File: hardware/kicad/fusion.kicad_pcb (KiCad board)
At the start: 2 copper layers, 0 parts

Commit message: 0603 footprints and SP3T
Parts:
- added C1: 4.7uF, Capacitor_SMD:C_0603_1608Metric_Pad1.08x0.95mm_HandSolder, F.Cu at (206.2, 99.8)
- added C2: 4.7uF, Capacitor_SMD:C_0603_1608Metric_Pad1.08x0.95mm_HandSolder, F.Cu at (201.3, 102.8)
- added C3: 0.1uF, Capacitor_SMD:C_0603_1608Metric_Pad1.08x0.95mm_HandSolder, F.Cu at (206.1, 102.8)
- added C4: 0.1uF, Capacitor_SMD:C_0603_1608Metric_Pad1.08x0.95mm_HandSolder, F.Cu at (196.5, 102.6)
- added C5: 0.1uF, Capacitor_SMD:C_0603_1608Metric_Pad1.08x0.95mm_HandSolder, F.Cu at (201.3, 105.8)
- added C6: 0.1uF, Capacitor_SMD:C_0603_1608Metric_Pad1.08x0.95mm_HandSolder, F.Cu at (196.5, 105.6)
- added C7: 0.1uF, Capacitor_SMD:C_0603_1608Metric_Pad1.08x0.95mm_HandSolder, F.Cu at (201.4, 99.8)
- added C8: 0.1uF, Capacitor_SMD:C_0603_1608Metric_Pad1.08x0.95mm_HandSolder, F.Cu at (196.5, 108.6)
- added D1: LED, LED_SMD:LED_0603_1608Metric_Pad1.05x0.95mm_HandSolder, F.Cu at (211.1, 99.8)
- added D2: LED, LED_SMD:LED_0603_1608Metric_Pad1.05x0.95mm_HandSolder, F.Cu at (201.4, 108.9)
- added J1: BATTERY, Fusion:JST, F.Cu at (187.5, 108.0)
- added J2: LSM6DSOX, Connector_PinHeader_2.54mm:PinHeader_1x06_P2.54mm_Horizontal, F.Cu at (173.7, 73.4)
- added J3: PICKIT, Connector_PinSocket_2.54mm:PinSocket_1x05_P2.54mm_Vertical, F.Cu at (189.7, 90.8)
- added J4: HC-05, Connector_PinHeader_2.54mm:PinHeader_1x05_P2.54mm_Horizontal, F.Cu at (192.9, 73.2)
- added J5: FLEX, Connector_PinHeader_2.54mm:PinHeader_2x05_P2.54mm_Horizontal, F.Cu at (173.7, 90.8)
- added J7: FTDI, Connector_PinSocket_2.54mm:PinSocket_1x06_P2.54mm_Vertical, F.Cu at (187.1, 73.4)
- added L1: 4.7uH, Inductor_SMD:L_0603_1608Metric_Pad1.05x0.95mm_HandSolder, F.Cu at (196.6, 99.7)
- added R1: 270R, Resistor_SMD:R_0603_1608Metric_Pad0.98x0.95mm_HandSolder, F.Cu at (197.6, 91.9)
- added R10: 10K, Resistor_SMD:R_0603_1608Metric_Pad0.98x0.95mm_HandSolder, F.Cu at (210.9, 102.8)
- added R2: 20K, Resistor_SMD:R_0603_1608Metric_Pad0.98x0.95mm_HandSolder, F.Cu at (203.7, 94.7)
- added R3: 10K, Resistor_SMD:R_0603_1608Metric_Pad0.98x0.95mm_HandSolder, F.Cu at (204.5, 91.8)
- added R4: 270R, Resistor_SMD:R_0603_1608Metric_Pad0.98x0.95mm_HandSolder, F.Cu at (210.9, 108.8)
- added R5: 10K, Resistor_SMD:R_0603_1608Metric_Pad0.98x0.95mm_HandSolder, F.Cu at (215.8, 99.8)
- added R6: 10K, Resistor_SMD:R_0603_1608Metric_Pad0.98x0.95mm_HandSolder, F.Cu at (215.7, 102.8)
- added R7: 10K, Resistor_SMD:R_0603_1608Metric_Pad0.98x0.95mm_HandSolder, F.Cu at (206.1, 105.8)
- added R8: 10K, Resistor_SMD:R_0603_1608Metric_Pad0.98x0.95mm_HandSolder, F.Cu at (210.9, 105.8)
- added R9: 10K, Resistor_SMD:R_0603_1608Metric_Pad0.98x0.95mm_HandSolder, F.Cu at (206.1, 108.8)
- added SW1: BUTTON, Button_Switch_THT:SW_PUSH_6mm_H5mm, F.Cu at (206.0, 72.9)
- added SW2: POWER, Button_Switch_SMD:SW_SP3T_PCM13, F.Cu at (177.3, 108.7)
- added SW3: UART, Button_Switch_THT:SW_CuK_JS202011CQN_DPDT_Straight, F.Cu at (162.6, 99.7)
- added U1: MCP1603, Package_TO_SOT_SMD:TSOT-23-5_HandSoldering, F.Cu at (196.6, 87.9)
- added U2: PIC16F690, Package_DIP:DIP-20_W7.62mm_Socket, F.Cu at (161.7, 73.2)

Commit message: Placing components
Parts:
- moved R6 74.3 mm to (143.0, 87.2), turned to -90 degrees
- moved R8 64.6 mm to (149.0, 87.2), turned to -90 degrees
- moved R7 62.9 mm to (146.0, 87.2), turned to -90 degrees
- moved R9 58.3 mm to (152.0, 87.2), turned to -90 degrees
- moved R10 58.1 mm to (155.0, 87.2), turned to -90 degrees
- moved C5 57.0 mm to (147.5, 87.2), turned to 90 degrees
- moved C4 54.2 mm to (144.5, 87.2), turned to 90 degrees
- moved D1 53.5 mm to (159.5, 85.7)
- moved R5 51.6 mm to (165.7, 87.4), turned to 180 degrees
- moved SW1 50.9 mm to (163.8, 101.2)
- moved J4 50.9 mm to (150.6, 101.4), turned to -90 degrees
- moved J3 49.7 mm to (140.4, 97.7), turned to 180 degrees
- moved C6 49.6 mm to (150.5, 87.2), turned to 90 degrees
- moved C7 49.6 mm to (153.5, 87.2), turned to 90 degrees
- moved J7 48.6 mm to (154.3, 109.2), turned to 90 degrees
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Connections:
- J5 pad 1: GNDREF -> THUMB
- J5 pad 10: THUMB -> GNDREF
- J5 pad 3: GNDREF -> INDEX
- J5 pad 5: GNDREF -> MIDDLE
- J5 pad 6: PINKY -> GNDREF
- J5 pad 8: MIDDLE -> GNDREF
- J5 pad 9: INDEX -> PINKY
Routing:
- added copper zone on B.Cu, net GNDREF
- added copper zone on F.Cu, net GNDREF
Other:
- board outline added: 133.6 x 59.7 mm

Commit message: Moving around components
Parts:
- moved J1 35.8 mm to (143.1, 105.0), turned to 0 degrees
- moved D2 33.0 mm to (171.1, 83.8), turned to 0 degrees
- moved R4 29.6 mm to (171.1, 85.4), turned to 180 degrees
- moved R3 21.7 mm to (153.3, 113.7)
- moved C3 21.0 mm to (149.9, 113.7), turned to 180 degrees
- moved SW3 18.5 mm to (173.2, 102.0), turned to -90 degrees
- moved J4 16.4 mm to (167.0, 101.4)
- moved SW1 10.9 mm to (153.4, 104.8), turned to -90 degrees
- moved J7 7.85 mm to (153.2, 101.4), turned to -90 degrees
- moved R5 0.92 mm to (165.0, 88.0)
- moved R2 0.78 mm to (161.5, 88.0)
- moved C1 0.60 mm to (168.4, 85.4)
- moved C2 0.60 mm to (163.1, 82.7)
- moved L1 0.60 mm to (160.4, 83.7)
- moved R1 0.60 mm to (158.5, 83.7)
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
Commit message: Route board
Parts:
- J4: footprint Connector_PinHeader_2.54mm:PinHeader_1x05_P2.54mm_Horizontal -> Connector_PinHeader_2.54mm:PinHeader_1x04_P2.54mm_Horizontal
- SW2: footprint Button_Switch_SMD:SW_SP3T_PCM13 -> Fusion:SP3T
- SW3: footprint Button_Switch_THT:SW_CuK_JS202011CQN_DPDT_Straight -> Fusion:SPDT
- moved D2 37.6 mm to (140.3, 105.3), turned to -90 degrees
- moved R4 35.3 mm to (142.0, 105.3), turned to 90 degrees
- moved SW2 24.1 mm to (150.9, 106.4), turned to 180 degrees
- moved SW3 10.3 mm to (162.9, 103.0), turned to 180 degrees
- moved SW1 9.09 mm to (148.9, 112.8), turned to 0 degrees
- moved J4 6.81 mm to (166.6, 108.2)
- moved J1 6.00 mm to (142.9, 111.0)
- moved C3 3.91 mm to (152.0, 110.4)
- moved R3 3.91 mm to (155.4, 110.4)
- moved C1 2.00 mm to (167.3, 87.1)
- moved U1 0.87 mm to (163.7, 85.0)
- moved L1 0.66 mm to (159.9, 84.1)
- moved D1 0.55 mm to (159.0, 86.5), turned to 180 degrees
- moved R1 0.43 mm to (158.4, 84.1)
- moved C2 0.37 mm to (162.8, 82.5)
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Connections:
- J4 pad 1: BT_KEY -> +3V3
- J4 pad 2: +3V3 -> GNDREF
- J4 pad 3: GNDREF -> BT_TX
- J4 pad 4: BT_TX -> BT_RX
- U2 pad 2: BT_KEY -> LED
- U2 pad 6: LED -> unconnected-(U2-Pad6)
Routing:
- net +3V3: track 0.00 -> 145.2 mm
- net Net-(C1-Pad1): track 0.00 -> 46.3 mm, vias 0 -> 2
- net BUTTON: track 0.00 -> 34.3 mm
- net CS: track 0.00 -> 27.9 mm
- net PINKY: track 0.00 -> 26.0 mm, vias 0 -> 1
- net THUMB: track 0.00 -> 23.4 mm, vias 0 -> 1
- net MOSI: track 0.00 -> 21.8 mm
- net VBAT_ADC: track 0.00 -> 18.8 mm
- net INDEX: track 0.00 -> 18.4 mm, vias 0 -> 1
- net RING: track 0.00 -> 18.4 mm, vias 0 -> 1
- net MIDDLE: track 0.00 -> 18.2 mm, vias 0 -> 1
- net MCLR: track 0.00 -> 16.8 mm, vias 0 -> 1
- net FTDI_TX: track 0.00 -> 13.4 mm
- net SCK: track 0.00 -> 13.2 mm
- net MISO: track 0.00 -> 13.2 mm
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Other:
- board size 133.6 x 59.7 mm -> 33 x 51.3 mm

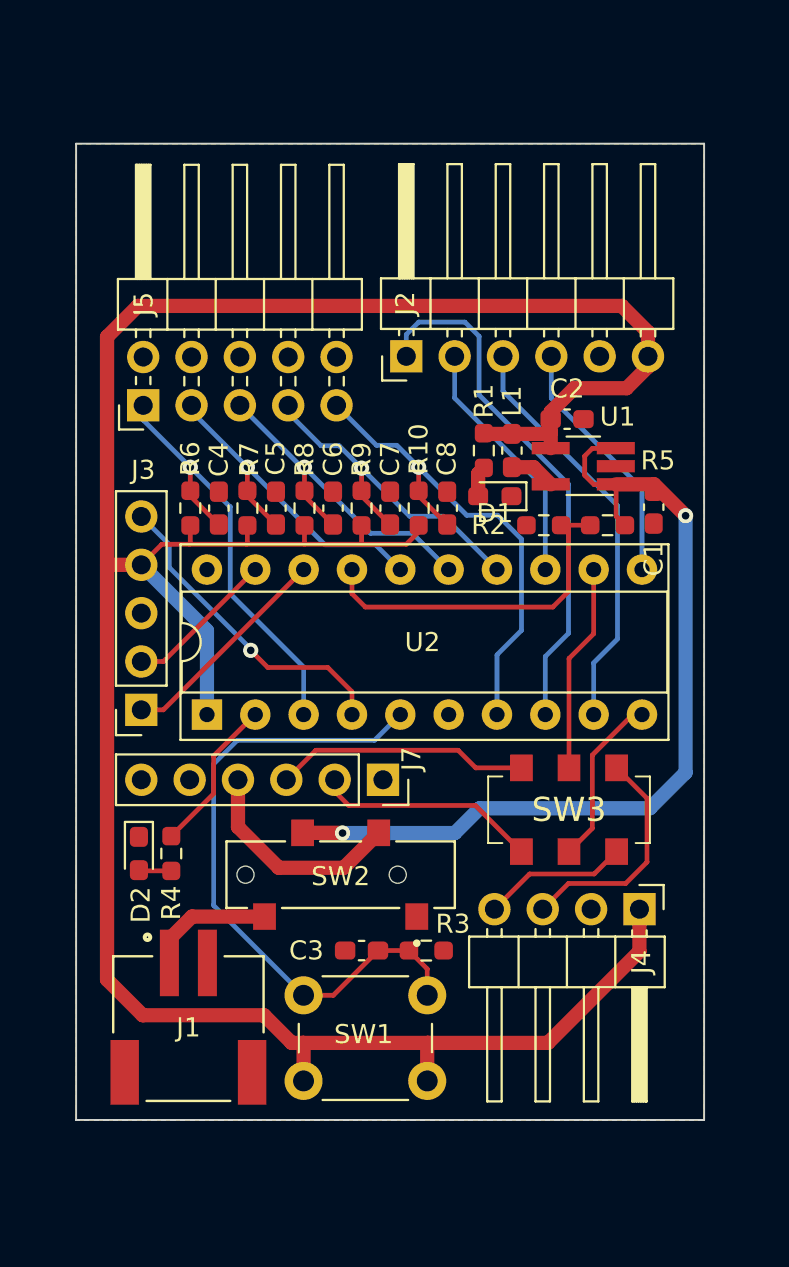
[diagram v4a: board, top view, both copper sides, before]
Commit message: Rounded corners, mounting holes, and DRC
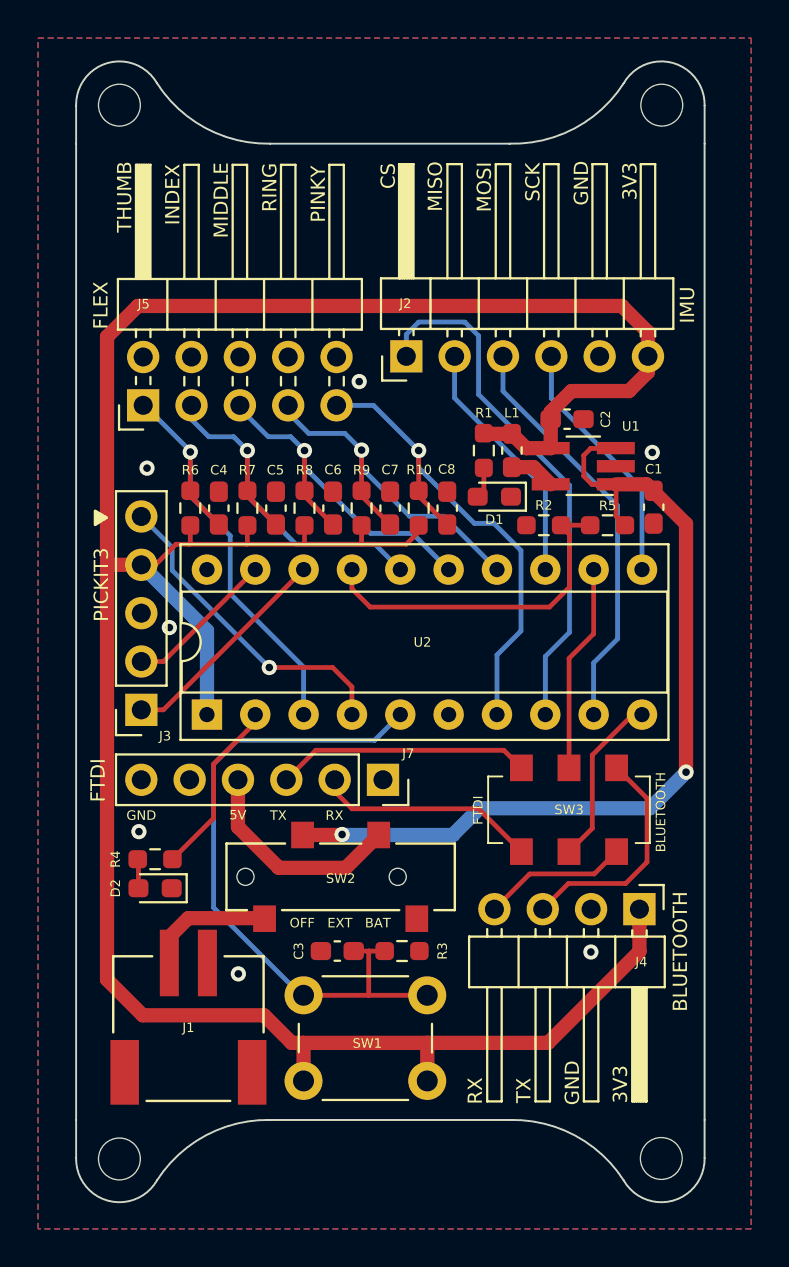
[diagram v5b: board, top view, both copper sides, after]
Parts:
- added REF**: MountingHole_2.2mm_M2_ISO7380, MountingHole:MountingHole_2.2mm_M2_ISO7380, F.Cu at (167.8, 121.3)
- added REF**: MountingHole_2.2mm_M2_ISO7380, MountingHole:MountingHole_2.2mm_M2_ISO7380, F.Cu at (139.3, 66.0)
- added REF**: MountingHole_2.2mm_M2_ISO7380, MountingHole:MountingHole_2.2mm_M2_ISO7380, F.Cu at (139.3, 121.3)
- added REF**: MountingHole_2.2mm_M2_ISO7380, MountingHole:MountingHole_2.2mm_M2_ISO7380, F.Cu at (167.8, 66.0)
- moved D2 2.01 mm to (141.2, 107.1), turned to 180 degrees
- moved C3 1.28 mm to (150.7, 110.4)
- moved R3 1.28 mm to (154.1, 110.4)
- moved R4 0.90 mm to (141.2, 105.6), turned to 0 degrees
- moved SW2 0.11 mm to (150.9, 106.5)
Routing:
- net INDEX: track 18.4 -> 20.9 mm
- net RING: track 18.4 -> 19.9 mm
- net MIDDLE: track 18.2 -> 19.7 mm
- net BUTTON: track 34.3 -> 35.5 mm
- net LED: track 8.23 -> 9.35 mm
- net PINKY: track 26.0 -> 27.0 mm
- net THUMB: track 23.4 -> 24.2 mm
- net GNDREF: vias 0 -> 7
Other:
- board size 33 x 51.3 mm -> 33 x 59.9 mm
- board text added: "3V3"
- board text added: "5V"
- board text added: "BLUETOOTH"
- board text added: "CS"
- board text added: "FLEX"
- board text added: "FTDI"
- board text added: "GND"
- board text added: "IMU"
- board text added: "INDEX"
- board text added: "MIDDLE"
- board text added: "MISO"
- board text added: "MOSI"
- board text added: "OFF EXT BAT"
- board text added: "PICKIT3"
- board text added: "PINKY"
- board text added: "RING"
- board text added: "RX"
- board text added: "SCK"
- board text added: "THUMB"
- board text added: "TX"

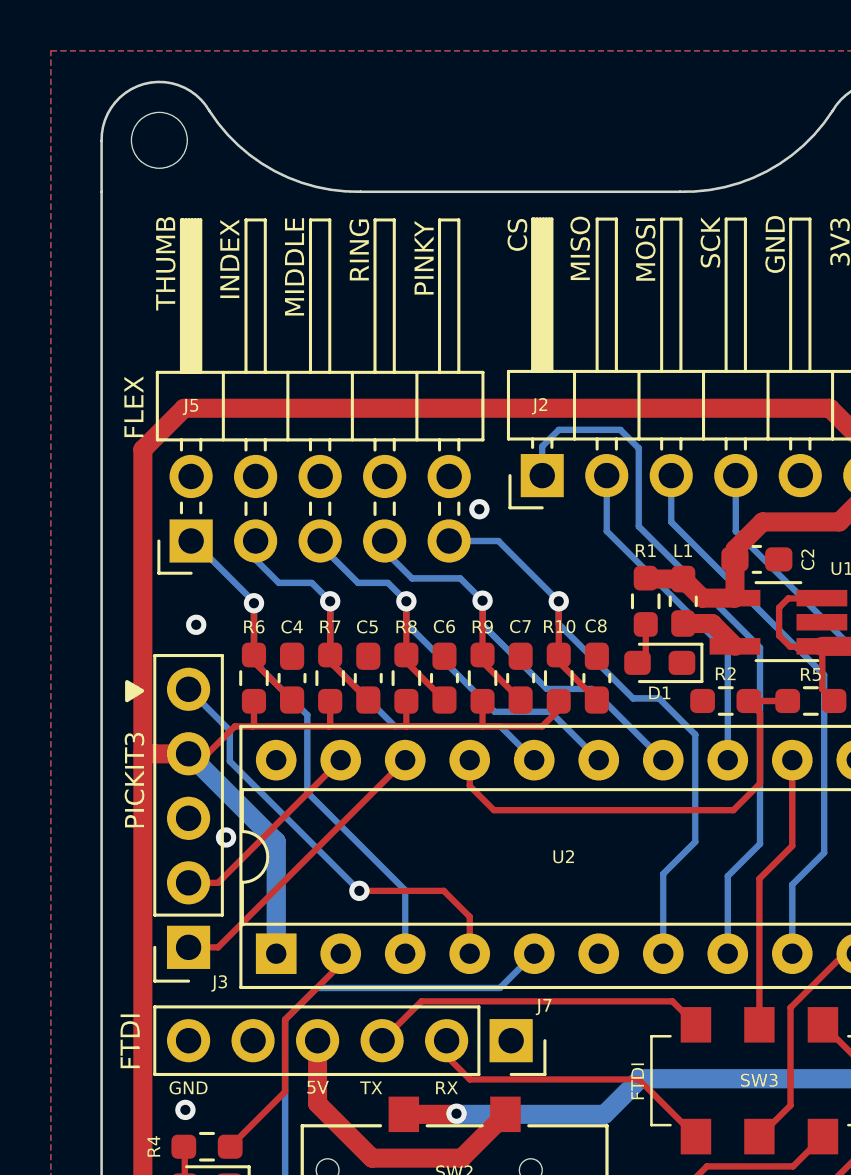
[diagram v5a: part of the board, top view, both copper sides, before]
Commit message: PCB cleanup and branding
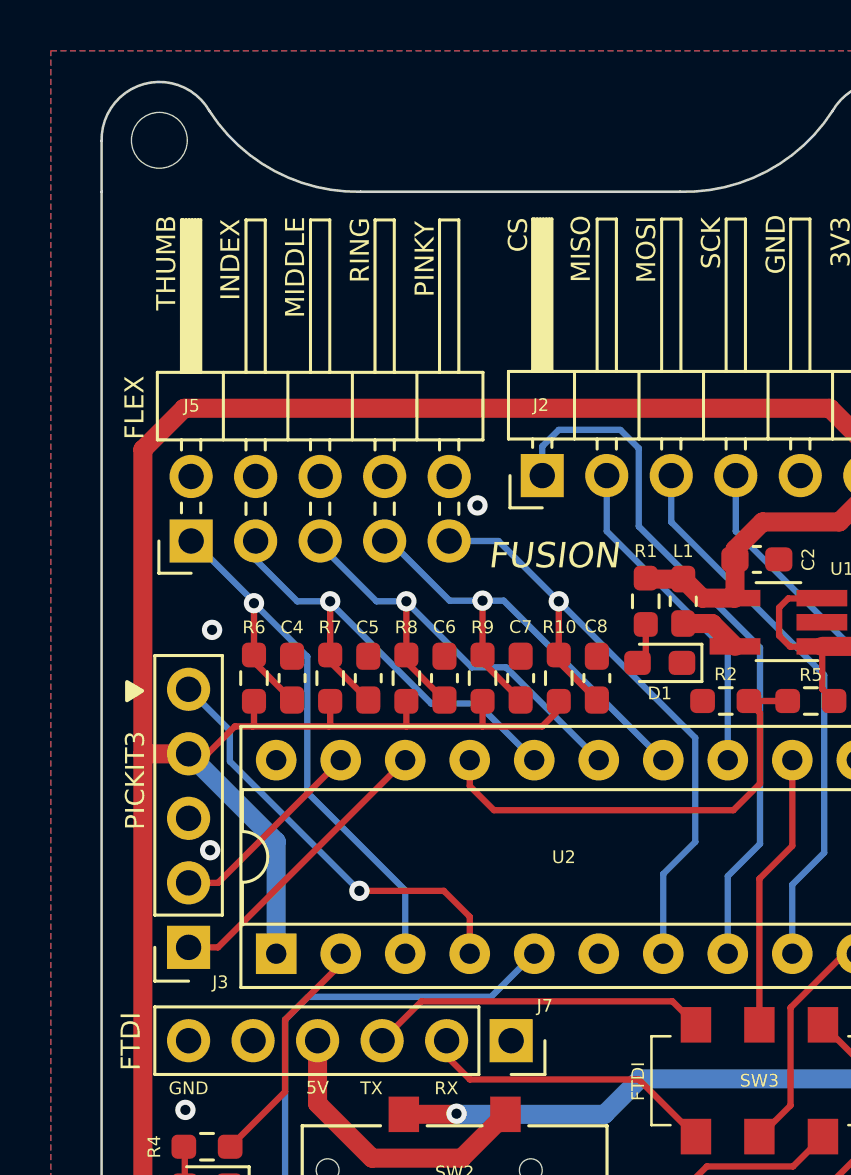
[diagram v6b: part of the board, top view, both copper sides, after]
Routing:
- net INDEX: track 20.9 -> 19.5 mm
- net RING: track 19.9 -> 19.1 mm
- net PINKY: track 27.0 -> 26.4 mm
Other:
- board text added: "FUSION"
